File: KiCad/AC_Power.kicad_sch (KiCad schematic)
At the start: 8 parts, among them J10 +230V_out, J9 +230V, K1 ?

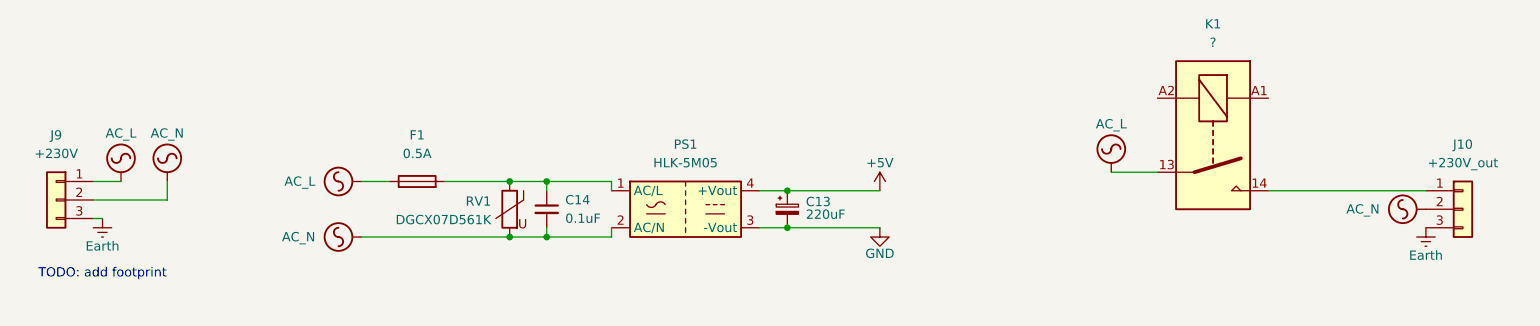
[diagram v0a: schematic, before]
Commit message: add 5v buck converter
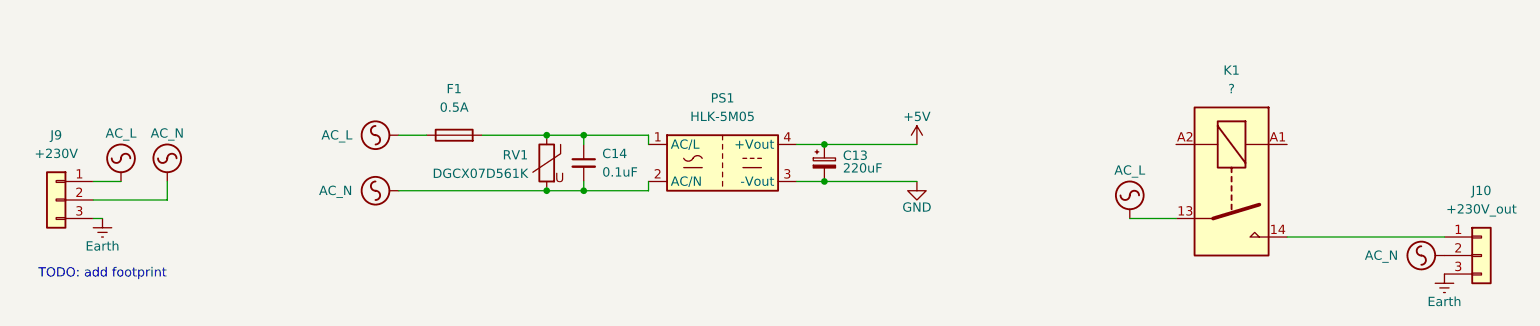
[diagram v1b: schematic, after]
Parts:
- J9: footprint TerminalBlock_Phoenix:TerminalBlock_Phoenix_MKDS-1,5-3-5.08_1x03_P5.08mm_Horizontal -> BarrierBlock_DORABO_1x3P9.5mm
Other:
- moved on the sheet: C13, C14, F1, J10, K1, PS1, RV1
